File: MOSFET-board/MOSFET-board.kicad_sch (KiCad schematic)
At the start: 4 parts, among them J1 PCIE-LP-01-01-F-DV-A-TR, J2 DB25_Female, U11 PCF8575_Breakout

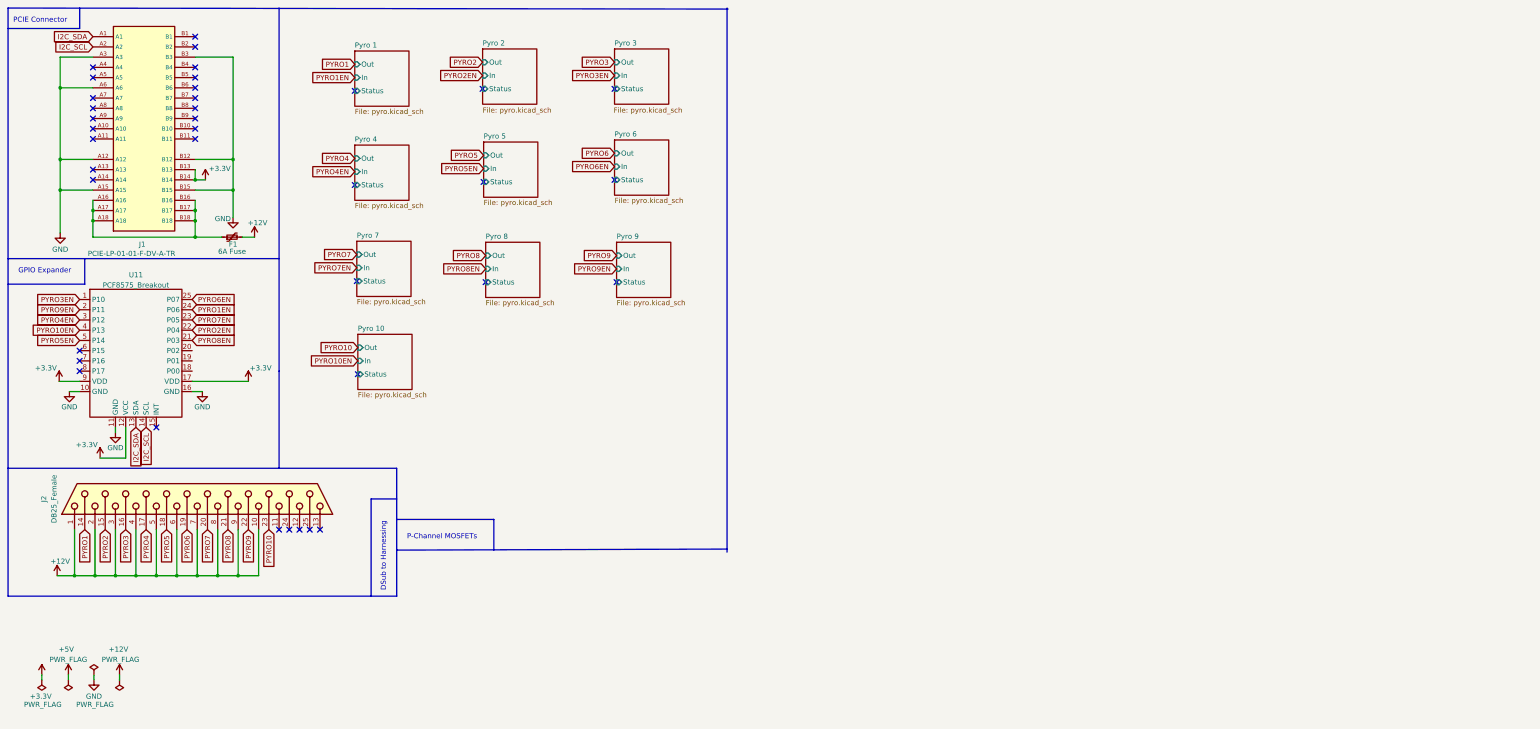
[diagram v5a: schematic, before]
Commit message: Finished mosfet layout
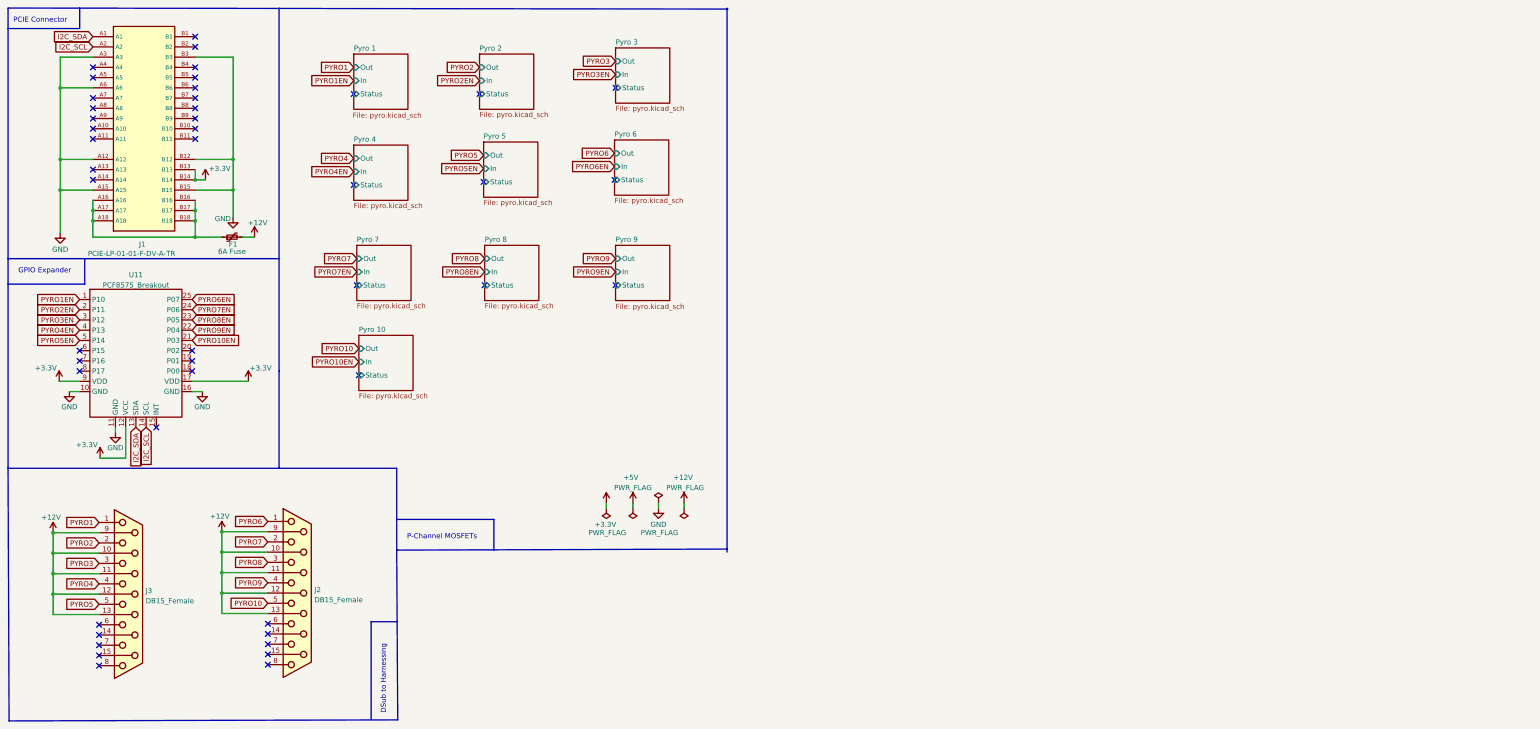
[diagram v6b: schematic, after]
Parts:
- removed J2: DB25_Female, Connector_Dsub:DSUB-25_Male_Horizontal_P2.77x2.84mm_EdgePinOffset7.70mm_Housed_MountingHolesOffset9.12mm, symbol Connector:DB25_Female
- added J2, J3: DB15_Female, Connector_Dsub:DSUB-15_Female_Horizontal_P2.77x2.84mm_EdgePinOffset7.70mm_Housed_MountingHolesOffset9.12mm, symbol Connector:DB15_Female
- F1: footprint Fuse:Fuse_0603_1608Metric -> Fuse:Fuse_2920_7451Metric
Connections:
- net +12V: now also J2.10 (P10), J2.11 (P111), J2.12 (P12), J2.13 (P13), J2.9 (P9), J3.10 (P10), J3.11 (P111), J3.12 (P12), J3.13 (P13), J3.9 (P9)
- net PYRO1: now also J3.1
- net PYRO10: now also J2.5
- net PYRO10EN: now also U11.21 (P03); no longer U11.4 (P13)
- net PYRO1EN: now also U11.1 (P10); no longer U11.24 (P06)
- net PYRO2: now also J3.2
- net PYRO2EN: now also U11.2 (P11); no longer U11.22 (P04)
- net PYRO3: now also J3.3
- net PYRO3EN: now also U11.3 (P12); no longer U11.1 (P10)
- net PYRO4: now also J3.4
- net PYRO4EN: now also U11.4 (P13); no longer U11.3 (P12)
- net PYRO5: now also J3.5
- net PYRO6: now also J2.1
- net PYRO7: now also J2.2
- net PYRO7EN: now also U11.24 (P06); no longer U11.23 (P05)
- net PYRO8: now also J2.3
- net PYRO8EN: now also U11.23 (P05); no longer U11.21 (P03)
- net PYRO9: now also J2.4
- net PYRO9EN: now also U11.22 (P04); no longer U11.2 (P11)
- no-connect marks 38 -> 46
